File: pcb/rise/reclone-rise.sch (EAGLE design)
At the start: 130 parts, among them Y1 12MHz, Y4 32K768

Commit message: Found alternate pins for video that were previously assigned to M0 and M1; tweaked headphone filter values to take advantage of close to 24mA max per pin
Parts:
- added R26, R28, R29, R30: 4K7, SparkFun-Passives:RESISTOR0603-RES
- C14, C15: value 47n -> 56n
- R16, R50: value 180 -> 150
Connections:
- removed net M3RESET: FPGAB3.IO_L54P_M3RESET_3
- removed net WIFI_INT: MCUG$3.PB5
- new net WIFI_INT_WAKE: MCUG$3.PB5, WIFI.IO16
- net +3V3: now also FPGAB2.IO_L13P_M1_2, FPGAB2.IO_L1N_M0_CMPMISO_2, R29.2, R30.2
- net FPGA_CONFIG_INIT_B: now also R30.1
- net FPGA_CONFIG_PROGRAM_B: now also R29.1
- net GND: now also R26.1, R28.1
- net M3CKE: now also R28.2
- net M3ODT: now also R26.2
- net VIDEO_D1: now also FPGAB2.IO_L14P_D11_2; no longer FPGAB2.IO_L13P_M1_2
- net VIDEO_D3: now also FPGAB2.IO_L14N_D12_2; no longer FPGAB2.IO_L1N_M0_CMPMISO_2
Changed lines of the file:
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@@
 <part name="SUPPLY32" library="supply2" deviceset="GND" device=""/>
 <part name="SUPPLY33" library="supply2" deviceset="GND" device=""/>
-<part name="R16" library="SparkFun-Passives" deviceset="RESISTOR" device="0603-RES" value="180"/>
-<part name="R50" library="SparkFun-Passives" deviceset="RESISTOR" device="0603-RES" value="180"/>
-<part name="C14" library="SparkFun-Passives" deviceset="CAP" device="0603-CAP" value="47n"/>
-<part name="C15" library="SparkFun-Passives" deviceset="CAP" device="0603-CAP" value="47n"/>
+<part name="R16" library="SparkFun-Passives" deviceset="RESISTOR" device="0603-RES" value="150"/>
+<part name="R50" library="SparkFun-Passives" deviceset="RESISTOR" device="0603-RES" value="150"/>
+<part name="C14" library="SparkFun-Passives" deviceset="CAP" device="0603-CAP" value="56n"/>
+<part name="C15" library="SparkFun-Passives" deviceset="CAP" device="0603-CAP" value="56n"/>
 <part name="R51" library="SparkFun-Passives" deviceset="RESISTOR" device="0603-RES" value="330"/>
 <part name="R52" library="SparkFun-Passives" deviceset="RESISTOR" device="0603-RES" value="330"/>
@@
 <part name="U$6" library="reclone-rise" deviceset="+1V8" device=""/>
 <part name="U$7" library="reclone-rise" deviceset="+1V2" device=""/>
+<part name="R26" library="SparkFun-Passives" deviceset="RESISTOR" device="0603-RES" value="4K7"/>
+<part name="R28" library="SparkFun-Passives" deviceset="RESISTOR" device="0603-RES" value="4K7"/>
+<part name="SUPPLY22" library="supply2" deviceset="GND" device=""/>
+<part name="SUPPLY23" library="supply2" deviceset="GND" device=""/>
+<part name="R29" library="SparkFun-Passives" deviceset="RESISTOR" device="0603-RES" value="4K7"/>
+<part name="+3V16" library="supply1" deviceset="+3V3" device=""/>
+<part name="+3V17" library="supply1" deviceset="+3V3" device=""/>
+<part name="+3V18" library="supply1" deviceset="+3V3" device=""/>
+<part name="R30" library="SparkFun-Passives" deviceset="RESISTOR" device="0603-RES" value="4K7"/>
+<part name="+3V24" library="supply1" deviceset="+3V3" device=""/>
 </parts>
 <sheets>
@@
 </segment>
 </net>
-<net name="WIFI_INT" class="0">
+<net name="WIFI_INT_WAKE" class="0">
 <segment>
 <pinref part="MCU" gate="G$3" pin="PB5"/>
@@
 <label x="215.9" y="111.76" size="1.778" layer="95"/>
 </segment>
+<segment>
+<pinref part="WIFI" gate="G$1" pin="IO16"/>
+<wire x1="266.7" y1="38.1" x2="269.24" y2="38.1" width="0.1524" layer="91"/>
+<label x="269.24" y="38.1" size="1.778" layer="95"/>
+</segment>
 </net>
 <net name="LED_ACT" class="0">
@@
 <instance part="U$6" gate="G$1" x="251.46" y="251.46"/>
 <instance part="U$7" gate="G$1" x="342.9" y="248.92"/>
+<instance part="R26" gate="G$1" x="287.02" y="66.04" rot="R180"/>
+<instance part="R28" gate="G$1" x="287.02" y="27.94" rot="R180"/>
+<instance part="SUPPLY22" gate="GND" x="294.64" y="63.5"/>
+<instance part="SUPPLY23" gate="GND" x="297.18" y="27.94"/>
+<instance part="R29" gate="G$1" x="198.12" y="119.38" rot="R90"/>
+<instance part="+3V16" gate="G$1" x="198.12" y="129.54"/>
+<instance part="+3V17" gate="G$1" x="190.5" y="111.76"/>
+<instance part="+3V18" gate="G$1" x="180.34" y="93.98"/>
+<instance part="R30" gate="G$1" x="193.04" y="25.4" rot="R90"/>
+<instance part="+3V24" gate="G$1" x="193.04" y="35.56"/>
 </instances>
 <busses>
@@
 <net name="FPGA_CONFIG_PROGRAM_B" class="0">
 <segment>
-<wire x1="160.02" y1="114.3" x2="165.1" y2="114.3" width="0.1524" layer="91"/>
 <label x="162.56" y="114.3" size="1.778" layer="95"/>
 <pinref part="FPGA" gate="B2" pin="PROGRAM_B_2"/>
+<pinref part="R29" gate="G$1" pin="1"/>
+<wire x1="160.02" y1="114.3" x2="198.12" y2="114.3" width="0.1524" layer="91"/>
 </segment>
 </net>
 <net name="FPGA_CONFIG_INIT_B" class="0">
 <segment>
-<wire x1="160.02" y1="20.32" x2="165.1" y2="20.32" width="0.1524" layer="91"/>
 <label x="162.56" y="20.32" size="1.778" layer="95"/>
 <pinref part="FPGA" gate="B2" pin="IO_L65P_INIT_B_2"/>
+<pinref part="R30" gate="G$1" pin="1"/>
+<wire x1="160.02" y1="20.32" x2="193.04" y2="20.32" width="0.1524" layer="91"/>
 </segment>
 </net>
@@
 <net name="M3CKE" class="0">
 <segment>
-<wire x1="271.78" y1="27.94" x2="276.86" y2="27.94" width="0.1524" layer="91"/>
 <label x="274.32" y="27.94" size="1.778" layer="95"/>
 <pinref part="FPGA" gate="B3" pin="IO_L53P_M3CKE_3"/>
+<pinref part="R28" gate="G$1" pin="2"/>
+<wire x1="271.78" y1="27.94" x2="281.94" y2="27.94" width="0.1524" layer="91"/>
 </segment>
 <segment>
@@
 </segment>
 </net>
-<net name="M3RESET" class="0">
-<segment>
-<wire x1="271.78" y1="22.86" x2="276.86" y2="22.86" width="0.1524" layer="91"/>
-<label x="274.32" y="22.86" size="1.778" layer="95"/>
-<pinref part="FPGA" gate="B3" pin="IO_L54P_M3RESET_3"/>
-</segment>
-</net>
 <net name="M3A11" class="0">
 <segment>
@@
 <net name="M3ODT" class="0">
 <segment>
-<wire x1="271.78" y1="66.04" x2="276.86" y2="66.04" width="0.1524" layer="91"/>
 <label x="274.32" y="66.04" size="1.778" layer="95"/>
 <pinref part="FPGA" gate="B3" pin="IO_L45N_M3ODT_3"/>
+<pinref part="R26" gate="G$1" pin="2"/>
+<wire x1="271.78" y1="66.04" x2="281.94" y2="66.04" width="0.1524" layer="91"/>
 </segment>
 <segment>
@@
 <junction x="279.4" y="167.64"/>
 </segment>
+<segment>
+<pinref part="R28" gate="G$1" pin="1"/>
+<wire x1="292.1" y1="27.94" x2="294.64" y2="27.94" width="0.1524" layer="91"/>
+<wire x1="294.64" y1="27.94" x2="294.64" y2="30.48" width="0.1524" layer="91"/>
+<pinref part="SUPPLY23" gate="GND" pin="GND"/>
+<wire x1="294.64" y1="30.48" x2="297.18" y2="30.48" width="0.1524" layer="91"/>
+</segment>
+<segment>
+<pinref part="R26" gate="G$1" pin="1"/>
+<pinref part="SUPPLY22" gate="GND" pin="GND"/>
+<wire x1="292.1" y1="66.04" x2="294.64" y2="66.04" width="0.1524" layer="91"/>
+</segment>
 </net>
 <net name="+3V3" class="0">
@@
 <junction x="342.9" y="182.88"/>
 </segment>
+<segment>
+<pinref part="+3V16" gate="G$1" pin="+3V3"/>
+<pinref part="R29" gate="G$1" pin="2"/>
+<wire x1="198.12" y1="127" x2="198.12" y2="124.46" width="0.1524" layer="91"/>
+</segment>
+<segment>
+<pinref part="FPGA" gate="B2" pin="IO_L1N_M0_CMPMISO_2"/>
+<pinref part="+3V17" gate="G$1" pin="+3V3"/>
+<wire x1="160.02" y1="109.22" x2="190.5" y2="109.22" width="0.1524" layer="91"/>
+</segment>
+<segment>
+<pinref part="FPGA" gate="B2" pin="IO_L13P_M1_2"/>
+<pinref part="+3V18" gate="G$1" pin="+3V3"/>
+<wire x1="160.02" y1="91.44" x2="180.34" y2="91.44" width="0.1524" layer="91"/>
+</segment>
+<segment>
+<pinref part="+3V24" gate="G$1" pin="+3V3"/>
+<pinref part="R30" gate="G$1" pin="2"/>
+<wire x1="193.04" y1="33.02" x2="193.04" y2="30.48" width="0.1524" layer="91"/>
+</segment>
 </net>
 <net name="GPIO08" class="0">
@@
 </segment>
 <segment>
-<pinref part="FPGA" gate="B2" pin="IO_L1N_M0_CMPMISO_2"/>
-<wire x1="160.02" y1="109.22" x2="165.1" y2="109.22" width="0.1524" layer="91"/>
-<label x="162.56" y="109.22" size="1.778" layer="95"/>
+<pinref part="FPGA" gate="B2" pin="IO_L14N_D12_2"/>
+<wire x1="160.02" y1="83.82" x2="165.1" y2="83.82" width="0.1524" layer="91"/>
+<label x="162.56" y="83.82" size="1.778" layer="95"/>
 </segment>
 </net>
@@
 </segment>
 <segment>
-<pinref part="FPGA" gate="B2" pin="IO_L13P_M1_2"/>
-<wire x1="160.02" y1="91.44" x2="165.1" y2="91.44" width="0.1524" layer="91"/>
-<label x="162.56" y="91.44" size="1.778" layer="95"/>
+<pinref part="FPGA" gate="B2" pin="IO_L14P_D11_2"/>
+<wire x1="160.02" y1="86.36" x2="165.1" y2="86.36" width="0.1524" layer="91"/>
+<label x="162.56" y="86.36" size="1.778" layer="95"/>
 </segment>
 </net>

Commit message: Routed WIFI_INT, the missing GPIO pin, and a pull-down on the ODT signal
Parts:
- R36: value 47K -> 10K
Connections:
- net WIFI_INT_WAKE renamed WIFI_INT
- net GPIO25: now also FPGAB0.IO_L63P_SCP7_0; no longer FPGAB0.IO_L66N_SCP0_0
- net GPIO29: now also FPGAB0.IO_L66N_SCP0_0; no longer FPGAB0.IO_L63P_SCP7_0
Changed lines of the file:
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@@
 <part name="+3V21" library="supply1" deviceset="+3V3" device=""/>
 <part name="R35" library="SparkFun-Passives" deviceset="RESISTOR" device="0603-RES" value="47K"/>
-<part name="R36" library="SparkFun-Passives" deviceset="RESISTOR" device="0603-RES" value="47K"/>
+<part name="R36" library="SparkFun-Passives" deviceset="RESISTOR" device="0603-RES" value="10K"/>
 <part name="+3V22" library="supply1" deviceset="+3V3" device=""/>
 <part name="SUPPLY28" library="supply2" deviceset="GND" device=""/>
@@
 </segment>
 </net>
-<net name="WIFI_INT_WAKE" class="0">
-<segment>
-<pinref part="MCU" gate="G$3" pin="PB5"/>
-<wire x1="213.36" y1="111.76" x2="215.9" y2="111.76" width="0.1524" layer="91"/>
-<label x="215.9" y="111.76" size="1.778" layer="95"/>
-</segment>
-<segment>
-<pinref part="WIFI" gate="G$1" pin="IO16"/>
-<wire x1="266.7" y1="38.1" x2="269.24" y2="38.1" width="0.1524" layer="91"/>
-<label x="269.24" y="38.1" size="1.778" layer="95"/>
-</segment>
-</net>
 <net name="LED_ACT" class="0">
 <segment>
@@
 </segment>
 </net>
+<net name="WIFI_INT" class="0">
+<segment>
+<pinref part="WIFI" gate="G$1" pin="IO16"/>
+<wire x1="266.7" y1="38.1" x2="269.24" y2="38.1" width="0.1524" layer="91"/>
+<label x="269.24" y="38.1" size="1.778" layer="95"/>
+</segment>
+<segment>
+<pinref part="MCU" gate="G$3" pin="PB5"/>
+<wire x1="213.36" y1="111.76" x2="215.9" y2="111.76" width="0.1524" layer="91"/>
+<label x="215.9" y="111.76" size="1.778" layer="95"/>
+</segment>
+</net>
 </nets>
 </sheet>
@@
 </segment>
 <segment>
-<pinref part="FPGA" gate="B0" pin="IO_L66N_SCP0_0"/>
-<wire x1="38.1" y1="17.78" x2="40.64" y2="17.78" width="0.1524" layer="91"/>
-<label x="40.64" y="17.78" size="1.778" layer="95"/>
+<pinref part="FPGA" gate="B0" pin="IO_L63P_SCP7_0"/>
+<wire x1="38.1" y1="35.56" x2="40.64" y2="35.56" width="0.1524" layer="91"/>
+<label x="40.64" y="35.56" size="1.778" layer="95"/>
 </segment>
 </net>
@@
 </segment>
 <segment>
-<pinref part="FPGA" gate="B0" pin="IO_L63P_SCP7_0"/>
-<wire x1="38.1" y1="35.56" x2="40.64" y2="35.56" width="0.1524" layer="91"/>
-<label x="40.64" y="35.56" size="1.778" layer="95"/>
+<pinref part="FPGA" gate="B0" pin="IO_L66N_SCP0_0"/>
+<wire x1="38.1" y1="17.78" x2="40.64" y2="17.78" width="0.1524" layer="91"/>
+<label x="40.64" y="17.78" size="1.778" layer="95"/>
 </segment>
 </net>

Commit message: Added values for two inductors and three ferrite beads
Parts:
- L1, L2, L3: value (none) -> BEAD
- L4, L5: value (none) -> 2u2
- L6: value (none) -> 4u7
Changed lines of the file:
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@@
 <part name="SUPPLY31" library="supply2" deviceset="GND" device=""/>
 <part name="F1" library="reclone-rise" deviceset="POLYFUSE" device=""/>
-<part name="L1" library="SparkFun-Passives" deviceset="INDUCTOR" device="0603"/>
-<part name="L2" library="SparkFun-Passives" deviceset="INDUCTOR" device="0603"/>
-<part name="L3" library="SparkFun-Passives" deviceset="INDUCTOR" device="0603"/>
+<part name="L1" library="SparkFun-Passives" deviceset="INDUCTOR" device="0603" value="BEAD"/>
+<part name="L2" library="SparkFun-Passives" deviceset="INDUCTOR" device="0603" value="BEAD"/>
+<part name="L3" library="SparkFun-Passives" deviceset="INDUCTOR" device="0603" value="BEAD"/>
 <part name="D1" library="SparkFun-DiscreteSemi" deviceset="DIODE-ZENER" device="5.6V" value="5.6V"/>
 <part name="SUPPLY32" library="supply2" deviceset="GND" device=""/>
@@
 <part name="SUPPLY41" library="supply2" deviceset="GND" device=""/>
 <part name="+3V27" library="supply1" deviceset="+3V3" device=""/>
-<part name="L4" library="SparkFun-Passives" deviceset="INDUCTOR" device="0603"/>
-<part name="L5" library="SparkFun-Passives" deviceset="INDUCTOR" device="0603"/>
-<part name="L6" library="SparkFun-Passives" deviceset="INDUCTOR" device="0603"/>
+<part name="L4" library="SparkFun-Passives" deviceset="INDUCTOR" device="0603" value="2u2"/>
+<part name="L5" library="SparkFun-Passives" deviceset="INDUCTOR" device="0603" value="2u2"/>
+<part name="L6" library="SparkFun-Passives" deviceset="INDUCTOR" device="0603" value="4u7"/>
 <part name="C17" library="SparkFun-Passives" deviceset="CAP" device="0603-CAP" value="10u"/>
 <part name="C18" library="SparkFun-Passives" deviceset="CAP" device="0603-CAP" value="10u"/>

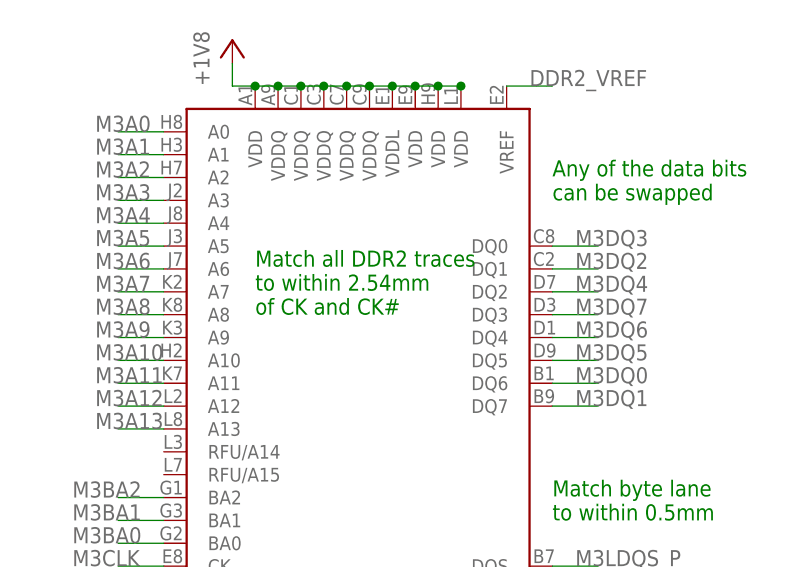
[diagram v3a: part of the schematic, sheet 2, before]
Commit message: Added some text on top of board
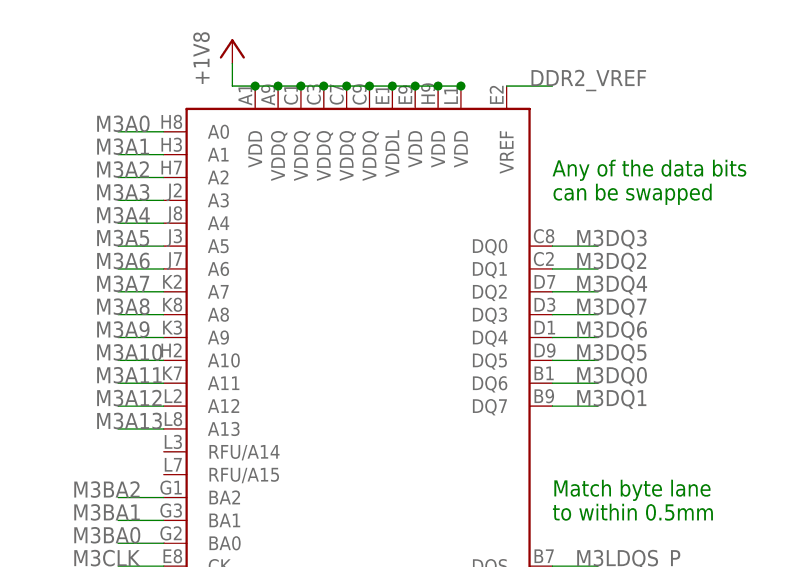
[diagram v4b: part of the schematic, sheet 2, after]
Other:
- note removed: "Match all DDR2 traces to within 2.54mm of CK and CK#"
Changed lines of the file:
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@@
 <text x="287.02" y="177.8" size="1.778" layer="91">Match DQS and DQS#
 within 0.254mm</text>
-<text x="254" y="220.98" size="1.778" layer="91">Match all DDR2 traces
-to within 2.54mm
-of CK and CK#</text>
 <text x="254" y="187.96" size="1.778" layer="91">Match CK and CK#
 within 0.254mm</text>

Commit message: Most of the way through consolidating BOM
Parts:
- removed C22, C51: 47u, SparkFun-Passives:CAP0603-CAP
- removed TXRX: AMBER, SparkFun-LED:LED0603
- added C8, C9: 100u, SparkFun-Passives:CAP_POL1206
- BOOT: value BOOT -> 1X2
- BUSPWR: value BUSPWR -> 1X2
- C14, C15: value 56n -> 47n
- C17, C18, C19: value 10u -> 4u7
- C3, C4: value 0u1 -> 0u47
- L4, L5: value 2u2 -> 4u7
- R14: value 220 -> 10K
- R16, R50: value 150 -> 165
- R19: value 4 -> 22
- R35: value 47K -> 10K
- R9: value 220 -> 160
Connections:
- removed net N$22: R14.2, TXRX.C
- removed net TXRX_LED: R14.1, USB-SERIAL.BCBUS3, USB-SERIAL.BCBUS4
- net +3V3: now also C9.+, R14.1; no longer C22.2, TXRX.A
- net +5V: now also C8.+; no longer C51.2
- net GND: now also C8.-, C9.-; no longer C22.1, C51.1
- net SD_CLK: now also R14.2
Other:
- moved on the sheet: C23, C24, C25, C26, C27, C28, C29, C30, C31, C32, C33, R14

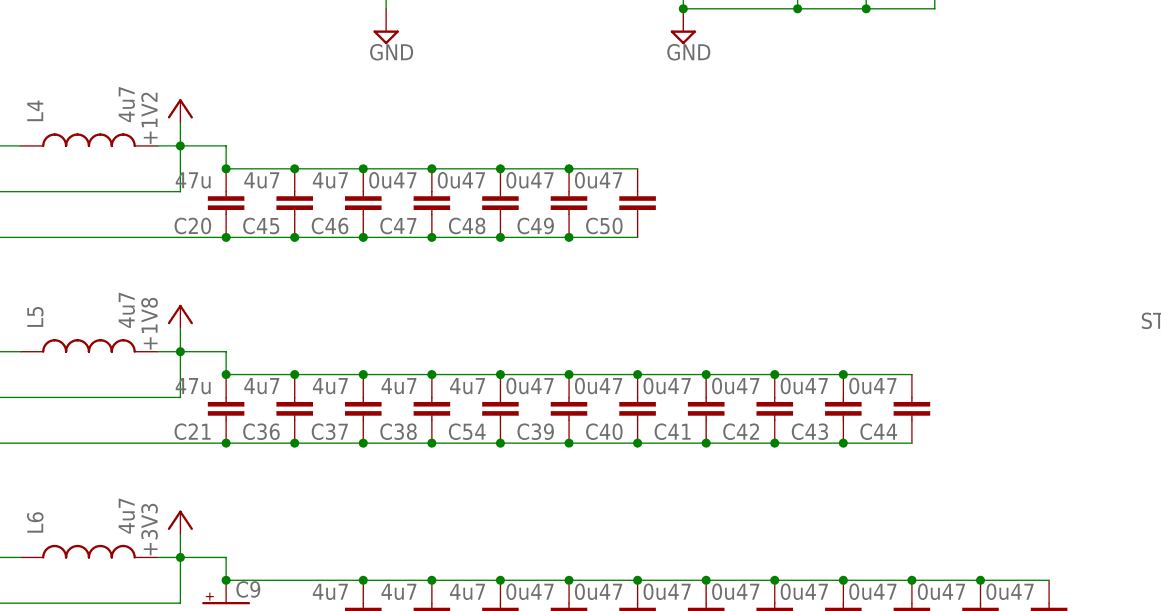
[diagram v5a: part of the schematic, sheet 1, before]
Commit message: Finished consolidating BOM; starting to populate Digikey info
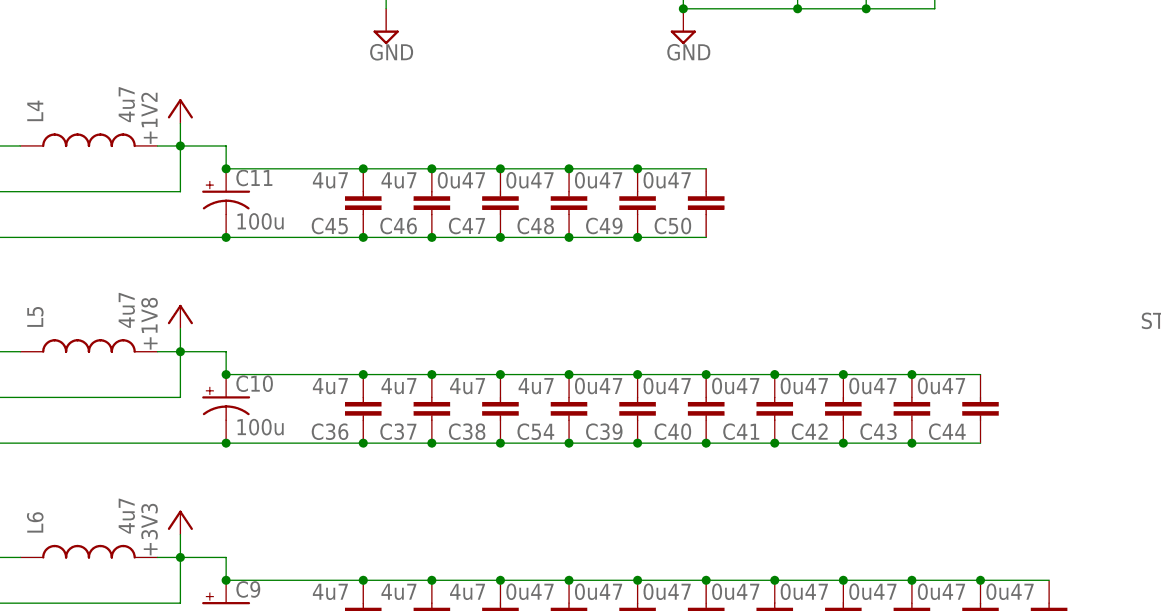
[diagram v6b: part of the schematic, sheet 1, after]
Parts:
- removed C20, C21: 47u, SparkFun-Passives:CAP0603-CAP
- added C10, C11: 100u, SparkFun-Passives:CAP_POL1206
- A/V: DIGIKEY# (none) -> CP-43514SJCT-ND; MANF (none) -> CUI Inc.; MANF# (none) -> SJ-43514-SMT-TR
- CFG: DIGIKEY# (none) -> 93LC46BT-I/OTCT-ND; MANF (none) -> Microchip Technology; MANF# (none) -> 93LC46BT-I/OT
- GPIO: DIGIKEY# (none) -> S2012EC-20-ND; MANF (none) -> Sullins Connector Solutions; MANF# (none) -> PREC020DAAN-RC
- OSC10M: DIGIKEY# (none) -> 631-1436-1-ND; MANF (none) -> Fox Electronics; MANF# (none) -> F535L-10
- RAM: DIGIKEY# (none) -> 1450-1141-ND; MANF (none) -> Alliance Memory, Inc.; MANF# (none) -> AS4C128M8D2-25BCN
- USB-SERIAL: DIGIKEY# (none) -> 768-1024-1-ND; MANF (none) -> FTDI, Future Technology Devices International Ltd; MANF# (none) -> FT2232HL-REEL
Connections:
- net +1V2: now also C11.+; no longer C20.2
- net +1V8: now also C10.+; no longer C21.2
- net GND: now also C10.-, C11.-; no longer C20.1, C21.1
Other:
- moved on the sheet: C36, C37, C38, C39, C40, C41, C42, C43, C44, C45, C46, C47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
